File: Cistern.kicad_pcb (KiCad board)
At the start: 2 copper layers, 55.5 x 79.6 mm, 16 parts, among them J2 Gauge Stepper, J3 Power Connector, Q1 BD244C, Q2 Gauge Calibration, SW1 WiFi reset, SW2 Water Sensor, U1 ULN2003A, U3 Boost Converter (5->20 V)

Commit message: Rebasing project on AISLER's design rules
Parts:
- removed BZ1: Buzzer, Cistern:AZDelivery_KY-012_Buzzer
- removed D1: Alarm Light, LED_THT:LED_D5.0mm
- removed D2: Pressure Sensor (4-20 mA), Connector_PinHeader_2.54mm:PinHeader_1x02_P2.54mm_Vertical
- removed D3: 3V, Diode_THT:D_A-405_P7.62mm_Horizontal
- removed J2: Gauge Stepper, Cistern:JST_XH_B5B-XH-A_1x05_P2.54mm_Vertical
- removed J3: Power Connector, TerminalBlock:TerminalBlock_bornier-2_P5.08mm
- removed MCU1: ~, Cistern:ESP32-NodeMCU
- removed Q1: BD244C, Package_TO_SOT_THT:TO-220-3_Vertical
- removed Q2: Gauge Calibration, Connector_PinHeader_2.54mm:PinHeader_1x02_P2.54mm_Vertical
- removed R1, R4: 150, Resistor_THT:R_Axial_DIN0207_L6.3mm_D2.5mm_P7.62mm_Horizontal
- removed R2: 68, Resistor_THT:R_Axial_DIN0207_L6.3mm_D2.5mm_P7.62mm_Horizontal
- removed SW1: WiFi reset, Button_Switch_THT:SW_PUSH_6mm
- removed SW2: Water Sensor, Connector_PinHeader_2.54mm:PinHeader_1x02_P2.54mm_Vertical
- removed U1: ULN2003A, Package_DIP:DIP-16_W7.62mm_Socket
- removed U3: Boost Converter (5->20 V), Cistern:DC-DC_Module_XL6009E1
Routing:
- net GND: track 238.7 -> 0.00 mm
- net +5V: track 139.7 -> 0.00 mm
- net Net-(MCU1-GPIO27): track 48.3 -> 0.00 mm
- net Net-(D2-K): track 48.3 -> 0.00 mm
- net Net-(MCU1-GPIO13): track 44.8 -> 0.00 mm
- net Net-(BZ1--): track 30.5 -> 0.00 mm
- net Net-(D2-A): track 15.5 -> 0.00 mm
- net Net-(MCU1-GPIO22): track 12.7 -> 0.00 mm
- net Net-(U1-O1): track 12.7 -> 0.00 mm
- net Net-(Q1-C): track 12.7 -> 0.00 mm
- net Net-(MCU1-GPIO19): track 12.3 -> 0.00 mm
- net Net-(MCU1-GPIO18): track 12.3 -> 0.00 mm
- net Net-(MCU1-RX2): track 11.2 -> 0.00 mm
- net Net-(MCU1-GPIO4): track 11.2 -> 0.00 mm
- net Net-(MCU1-TX2): track 11.2 -> 0.00 mm
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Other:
- board outline removed

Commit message: Starting PCB layout
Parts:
- added BZ1: Buzzer, Cistern:AZDelivery_KY-012_Buzzer, F.Cu at (96.5, 125.7)
- added D1: Alarm Light, LED_THT:LED_D5.0mm, B.Cu at (114.3, 113.0)
- added D2: Pressure, Connector_PinHeader_2.54mm:PinHeader_1x02_P2.54mm_Vertical, F.Cu at (102.9, 118.1)
- added D3: 3V, Diode_THT:D_A-405_P7.62mm_Horizontal, F.Cu at (108.0, 59.7)
- added J2: Gauge Stepper, Cistern:JST_XH_B5B-XH-A_1x05_P2.54mm_Vertical, F.Cu at (104.1, 97.8)
- added J3: Power Connector, TerminalBlock:TerminalBlock_bornier-2_P5.08mm, F.Cu at (121.9, 129.5)
- added MCU1: ~, Cistern:ESP32-NodeMCU, F.Cu at (123.2, 50.8)
- added Q1: BD244C, Package_TO_SOT_THT:TO-220-3_Vertical, F.Cu at (105.4, 123.2)
- added Q2: Gauge Cal., Connector_PinHeader_2.54mm:PinHeader_1x02_P2.54mm_Vertical, F.Cu at (90.2, 115.6)
- added R1: 150, Resistor_THT:R_Axial_DIN0207_L6.3mm_D2.5mm_P7.62mm_Horizontal, F.Cu at (108.0, 66.0)
- added R2: 68, Resistor_THT:R_Axial_DIN0207_L6.3mm_D2.5mm_P7.62mm_Horizontal, F.Cu at (106.7, 110.5)
- added R4: 150, Resistor_THT:R_Axial_DIN0207_L6.3mm_D2.5mm_P7.62mm_Horizontal, F.Cu at (101.6, 110.5)
- added SW1: WiFi reset, Button_Switch_THT:SW_PUSH_6mm, F.Cu at (88.2, 104.1)
- added SW2: Water, Connector_PinHeader_2.54mm:PinHeader_1x02_P2.54mm_Vertical, F.Cu at (96.5, 115.6)
- added U1: ULN2003A, Package_DIP:DIP-16_W7.62mm_Socket, F.Cu at (106.7, 82.5)
- added U3: Boost Converter (5->20 V), Cistern:DC-DC_Module_XL6009E1, F.Cu at (111.8, 122.5)
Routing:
- net GND: track 0.00 -> 126.0 mm
- net +5V: track 0.00 -> 124.1 mm, vias 0 -> 2
- net Net-(BZ1--): track 0.00 -> 87.7 mm, vias 0 -> 2
- net Net-(MCU1-GPIO13): track 0.00 -> 57.8 mm
- net Net-(D2-K): track 0.00 -> 49.3 mm, vias 0 -> 1
- net Net-(D1-A): track 0.00 -> 22.1 mm, vias 0 -> 1
- net Net-(Q1-B): track 0.00 -> 13.2 mm
- net Net-(U1-O1): track 0.00 -> 12.7 mm
- net Net-(Q1-C): track 0.00 -> 8.79 mm
- net Net-(MCU1-GPIO18): track 0.00 -> 7.93 mm
- net Net-(MCU1-GPIO19): track 0.00 -> 7.93 mm
- net Net-(J2-Pin_4): track 0.00 -> 7.62 mm
- net Net-(J2-Pin_3): track 0.00 -> 7.62 mm
- net Net-(J2-Pin_2): track 0.00 -> 7.62 mm
- net Net-(J2-Pin_1): track 0.00 -> 7.62 mm
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- added copper zone on B.Cu, net GND
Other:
- board outline added: 57.2 x 83.8 mm

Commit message: Finishing first version of board layout
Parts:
- added NPTH: MountingHole_4.5mm, MountingHole:MountingHole_4.5mm, F.Cu at (125.7, 128.3)
- added NPTH: MountingHole_4.5mm, MountingHole:MountingHole_4.5mm, F.Cu at (94.0, 63.5)
- D2: value Pressure -> Pressure Sensor (4-20 mA)
- Q2: value Gauge Cal. -> Gauge Calibration
- SW2: value Water -> Water Sensor
- moved J3 8.89 mm to (113.0, 129.5)
- moved Q2 6.35 mm to (96.5, 115.6)
- moved SW2 5.08 mm to (101.6, 115.6)
- moved D2 3.81 mm to (106.7, 118.1)
- moved MCU1 2.54 mm to (125.7, 50.8)
- moved D3 2.54 mm to (110.5, 59.7)
- moved R1 2.54 mm to (110.5, 66.0)
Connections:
- MCU1 pad 14: unconnected-(MCU1-GND-Pad14) -> GND
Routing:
- net Net-(MCU1-GPIO27): track 0.00 -> 114.1 mm
- net GND: track 126.0 -> 221.6 mm
- net Net-(MCU1-GPIO22): track 0.00 -> 61.9 mm
- net Net-(D2-K): track 49.3 -> 106.0 mm
- net Net-(D2-A): track 0.00 -> 49.3 mm
- net +5V: track 124.1 -> 112.8 mm, vias 2 -> 0
- net Net-(D1-A): track 22.1 -> 12.0 mm, vias 1 -> 0
- net Net-(BZ1--): track 87.7 -> 80.1 mm
- net Net-(MCU1-GPIO13): track 57.8 -> 61.5 mm
- net Net-(MCU1-GPIO18): track 7.93 -> 10.5 mm
- net Net-(MCU1-GPIO19): track 7.93 -> 9.72 mm
- net Net-(MCU1-RX2): track 6.88 -> 7.93 mm
- net Net-(Q1-B): track 13.2 -> 14.3 mm
- net Net-(MCU1-TX2): track 6.88 -> 7.93 mm
- net Net-(MCU1-GPIO4): track 6.88 -> 7.93 mm
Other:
- board size 57.2 x 83.8 mm -> 47 x 83.8 mm
- board text added: "Smart Cistern v1"
- board text added: "www.github.com/patridu/Cistern-Hardware"

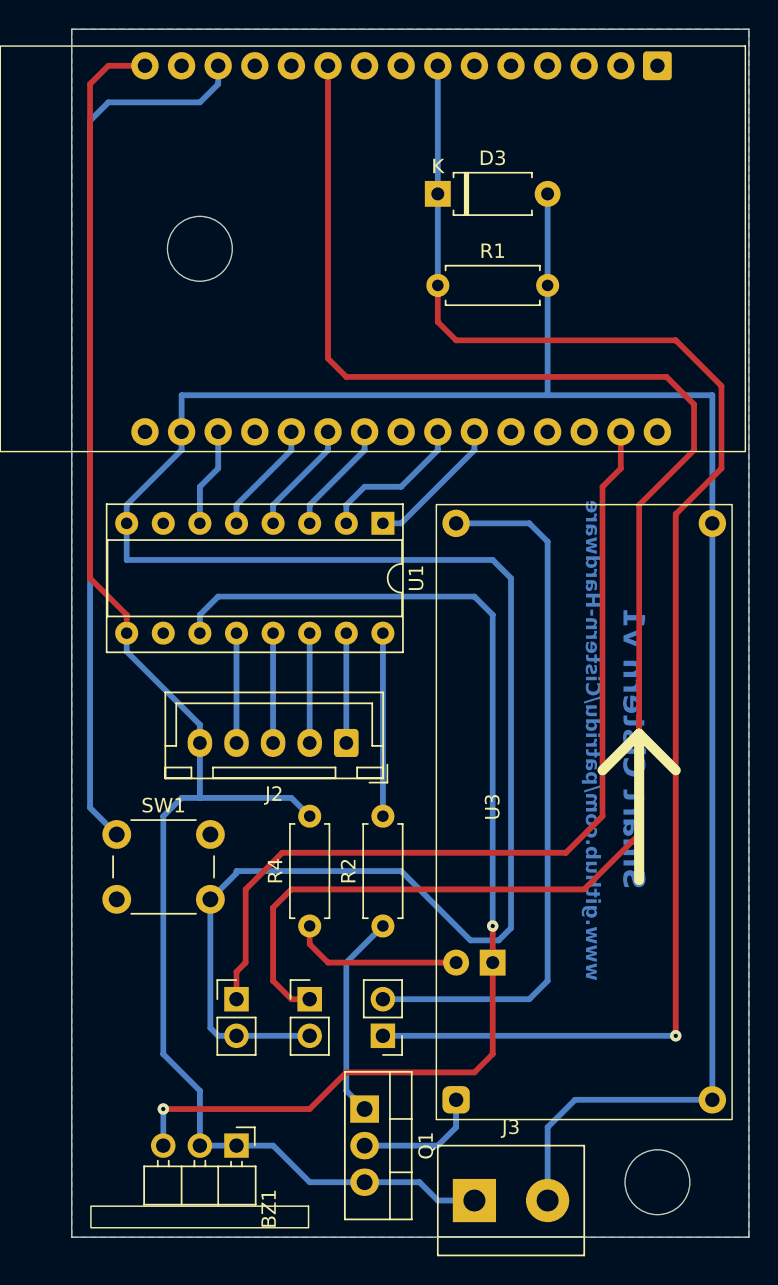
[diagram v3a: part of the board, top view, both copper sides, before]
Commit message: Minor improvements, ensuring design rules
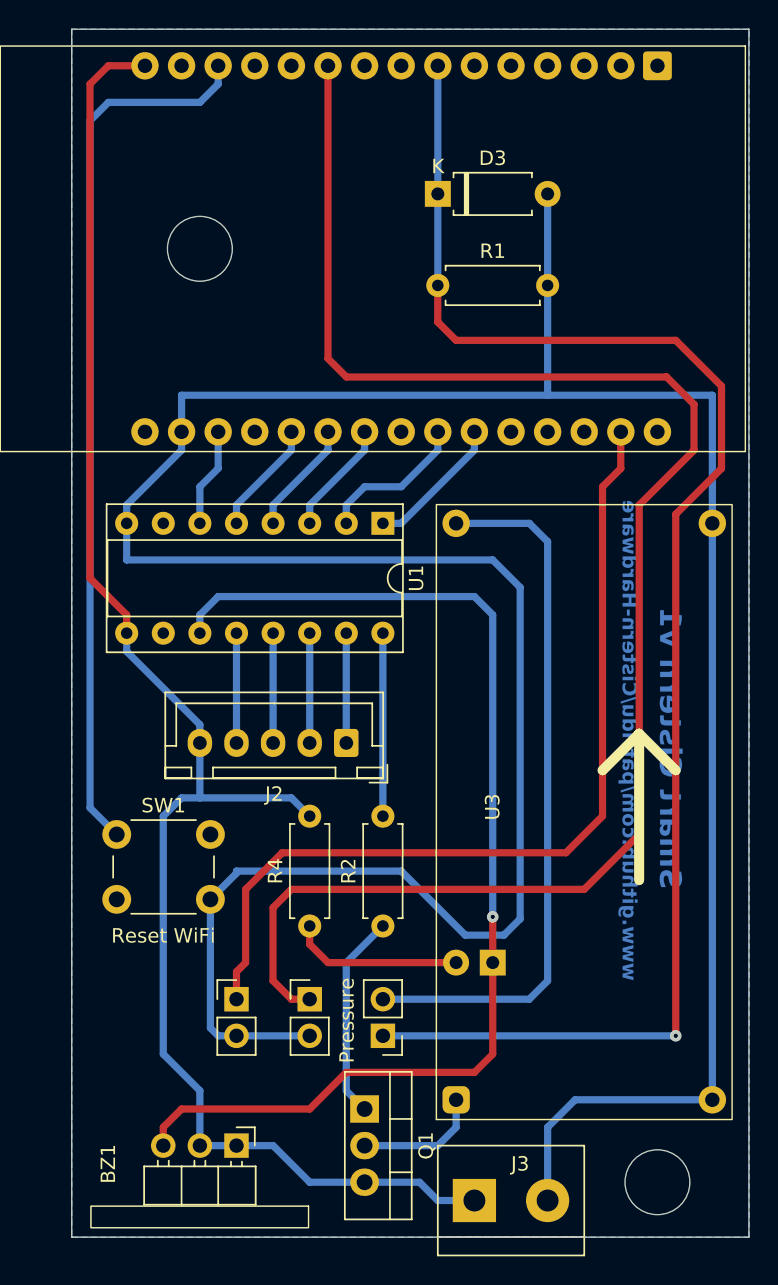
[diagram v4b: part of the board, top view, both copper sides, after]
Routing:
- net Net-(BZ1--): track 80.1 -> 79.4 mm, vias 2 -> 1
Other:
- board text added: "Pressure"
- board text added: "Reset WiFi"

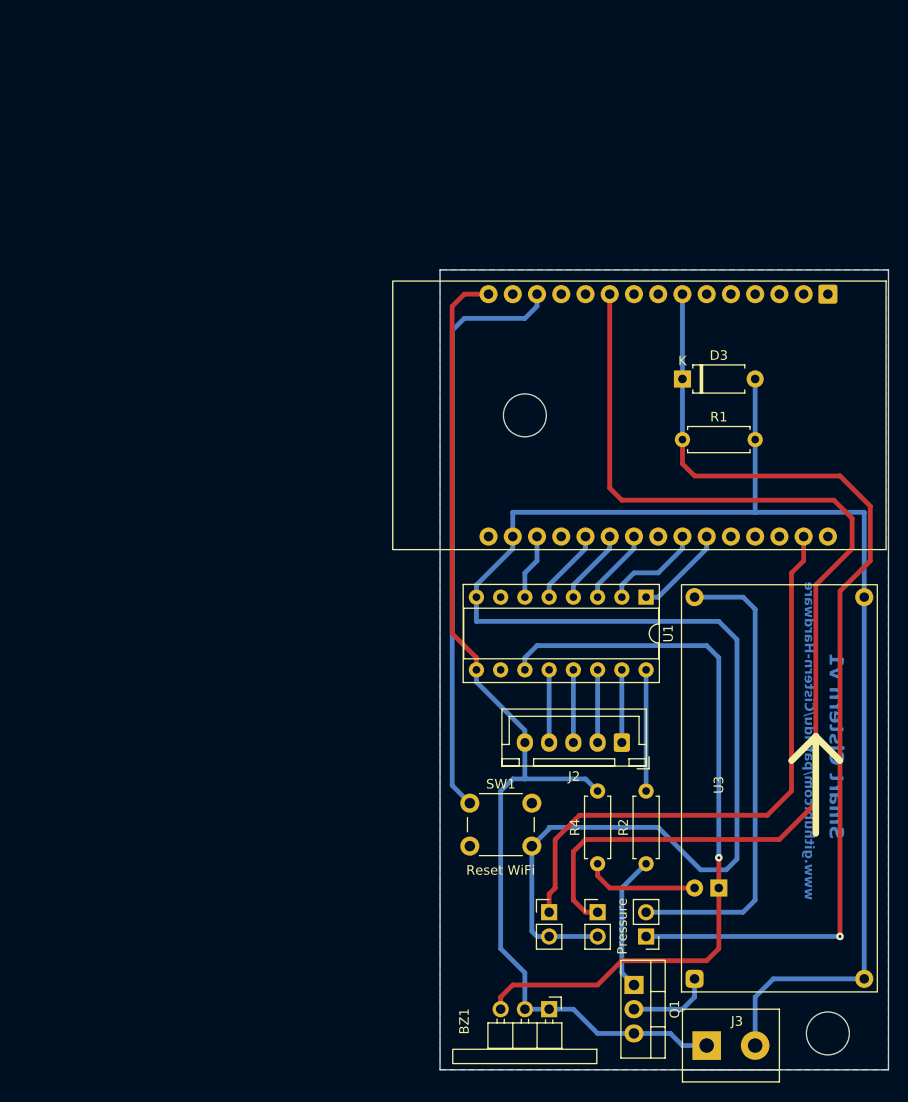
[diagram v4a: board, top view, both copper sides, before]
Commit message: Improving design some more, fixing custom footprints
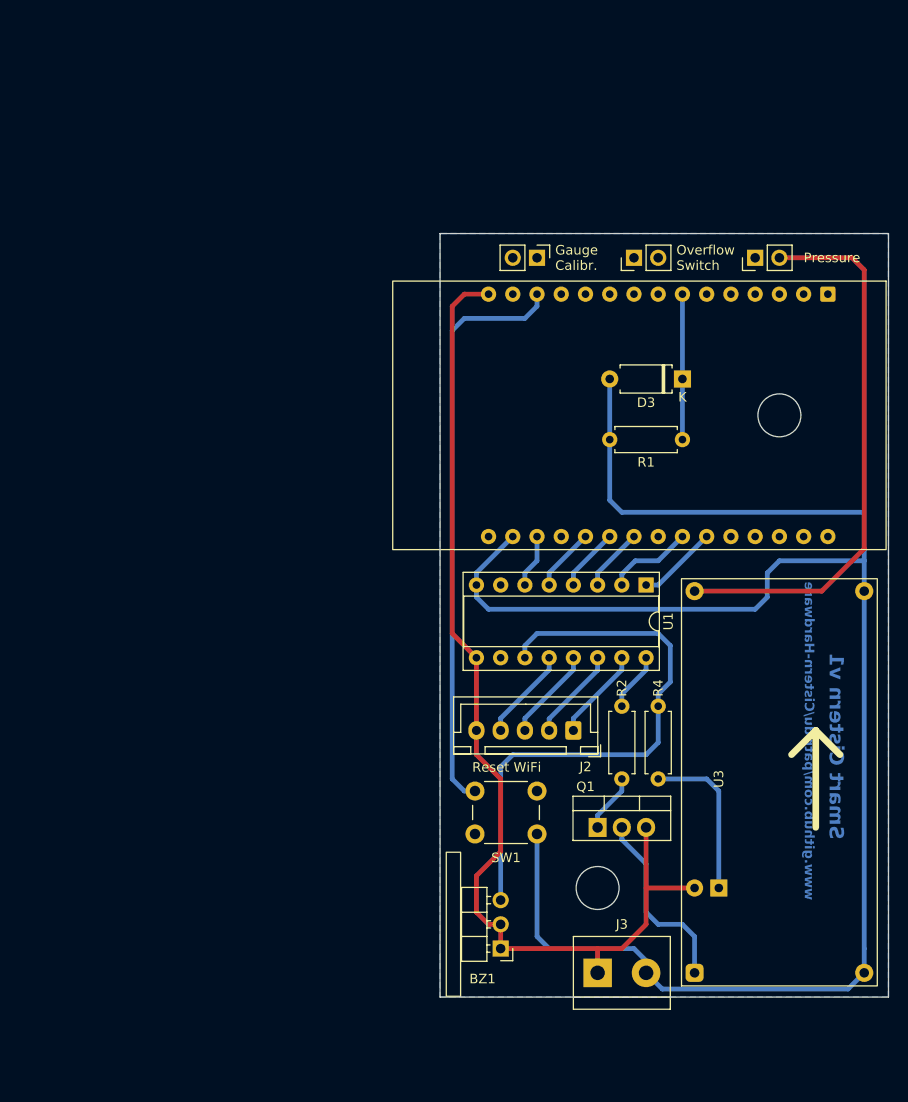
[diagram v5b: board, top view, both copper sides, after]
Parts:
- moved D2 72.0 mm to (118.1, 47.0), turned to 90 degrees
- moved SW2 68.7 mm to (105.4, 47.0), turned to 90 degrees
- moved Q2 68.6 mm to (95.2, 47.0), turned to -90 degrees
- moved NPTH 28.5 mm to (101.6, 113.0)
- moved NPTH 26.7 mm to (120.7, 63.5)
- moved R4 17.7 mm to (108.0, 94.0), turned to -90 degrees
- moved Q1 16.9 mm to (101.6, 106.7), turned to 0 degrees
- moved J3 13.7 mm to (101.6, 121.9)
- moved R2 9.25 mm to (104.1, 101.6)
- moved BZ1 8.13 mm to (91.4, 119.4), turned to 180 degrees
- moved J2 5.24 mm to (99.1, 96.5)
- moved SW1 1.38 mm to (88.8, 102.9)
- moved U1 1.27 mm to (106.7, 81.3)
- moved U3 0.63 mm to (111.8, 121.9)
- turned D3 to 180 degrees
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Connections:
- D1 pad 1: Net-(BZ1--) -> Net-(D1-K)
- D1 pad 2: Net-(D1-A) -> +5V
- R4 pad 1: Net-(D1-A) -> Net-(BZ1--)
- R4 pad 2: +5V -> Net-(D1-K)
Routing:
- net Net-(MCU1-GPIO27): track 114.1 -> 0.00 mm
- net Net-(D2-K): track 106.0 -> 15.2 mm, vias 1 -> 0
- net Net-(MCU1-GPIO22): track 61.9 -> 0.00 mm
- net GND: track 221.8 -> 189.6 mm
- net Net-(BZ1--): track 79.4 -> 59.8 mm, vias 1 -> 0
- net Net-(D1-K): track 0.00 -> 17.0 mm
- net Net-(D1-A): track 12.0 -> 0.00 mm
- net Net-(Q1-C): track 8.79 -> 19.9 mm
- net Net-(D2-A): track 49.3 -> 58.2 mm
- net Net-(Q1-B): track 14.3 -> 6.13 mm
- net Net-(U1-O1): track 12.7 -> 6.13 mm
- net +5V: track 112.8 -> 110.7 mm
- net Net-(J2-Pin_4): track 7.62 -> 9.72 mm
- net Net-(J2-Pin_3): track 7.62 -> 9.72 mm
- net Net-(J2-Pin_2): track 7.62 -> 9.72 mm
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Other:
- board size 47 x 83.8 mm -> 47 x 80 mm
- board text added: "Gauge Calibr."
- board text added: "Overflow Switch"

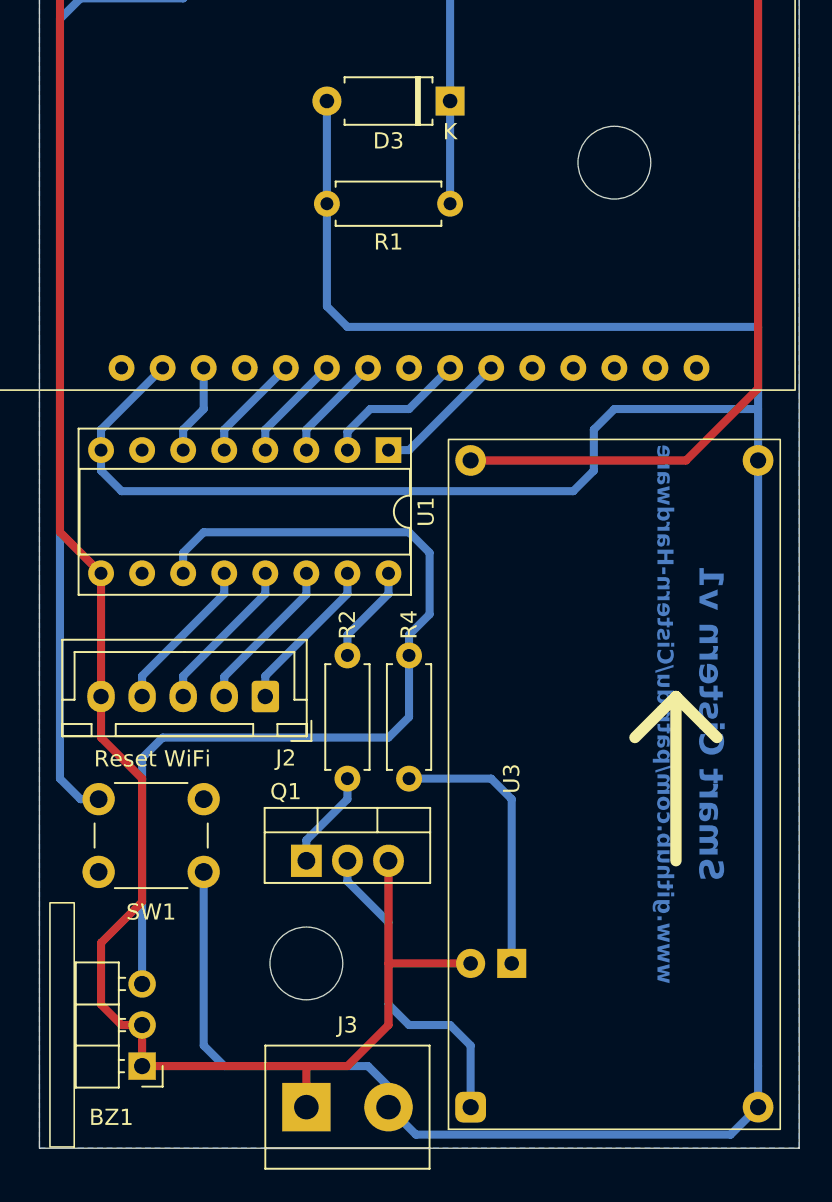
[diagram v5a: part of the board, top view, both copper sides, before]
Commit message: Adding teardrops
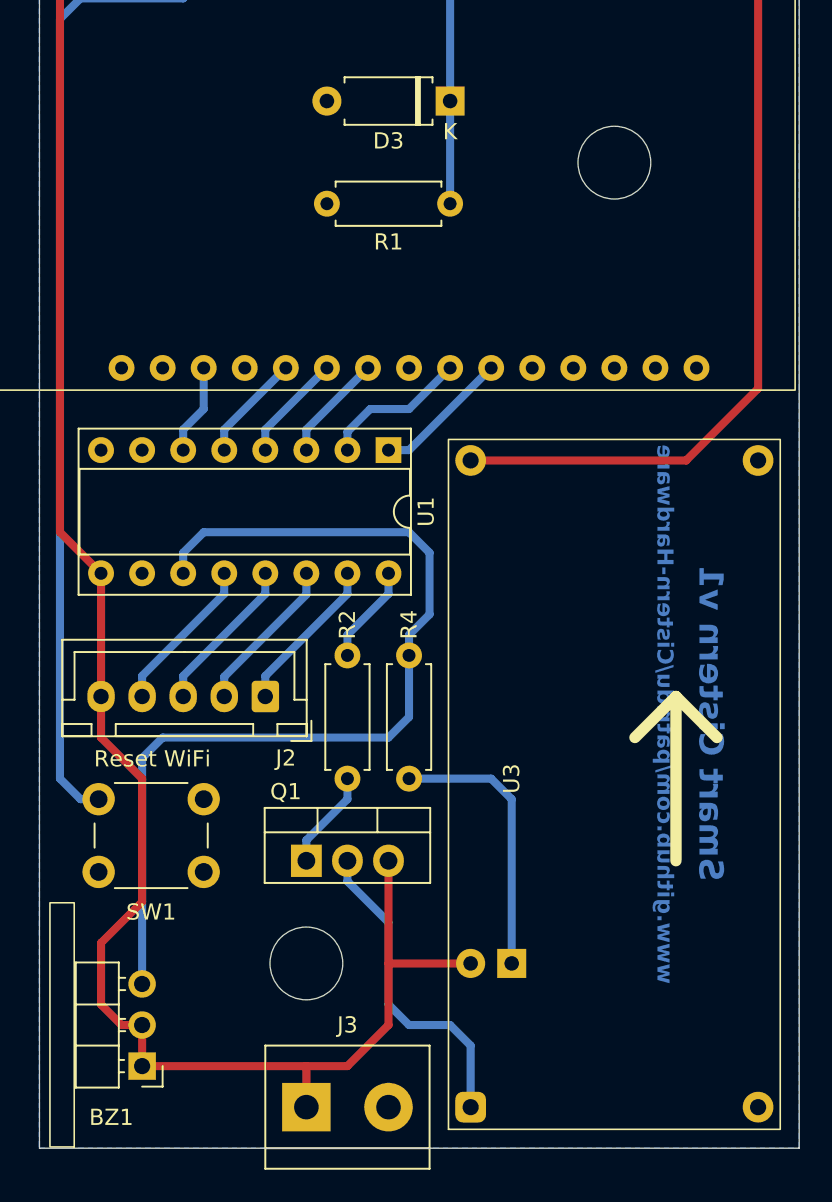
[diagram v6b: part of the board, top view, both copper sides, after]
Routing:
- net GND: track 189.6 -> 1.27 mm
